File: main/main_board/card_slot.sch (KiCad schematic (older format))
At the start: 6 parts, among them J3 Decimate, P1 my_pcie_8x

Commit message: Checkpoint of state before I start schematic revisions for the next version of the input board. There are not any substantive modifications to the input board, but some broad changes in component attributes related enabling a fabrication quote.
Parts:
- removed C29, C30: 100nF, Capacitor_SMD:C_0603_1608Metric, symbol Device:C_Small
- removed J3: Decimate, Connector_PinHeader_2.00mm:PinHeader_2x02_P2.00mm_Vertical_SMD, symbol Connector_Generic:Conn_02x02_Odd_Even
- removed R27, R28: 3.3K, Resistor_SMD:R_0603_1608Metric, symbol Device:R_US
- P1: footprint input:BUS_PCIexpress_x8 -> input:PCIE_8x_female; Description Do Not Populate -> (none); MPN DNP -> (none)
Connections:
- net labels added: +10V, +5VANA, +5VDIG, -6V, SYNC
- net labels removed: OVDD, RAW_+10V, RAW_+5VANA, RAW_+5VDIG, RAW_-6V, SEL0, SEL1, SYNC_IN
- wire segments 177 -> 155
- no-connect marks 10 -> 7
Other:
- note added: "Connector for a single input board"
- note removed: "Connector is oriented with the low number pins toward\nthe back of the board. Working forward, we have\n -- High speed LVDS signals\n -- Digital supply\n -- Low speed digital signals\n -- Analog supplies\n -- Analog signals\n\nThere are many grounds\n"
- note removed: "Selects the down-sampling factor for the ADC digital filter. \nOn the LTC2512/24 down-sampling factors of 4, 8, 16 and 32 \nare selected for [SEL1 SEL0] combinations of \n00, 01, 10 and 11 respectively."
- note removed: "The connector to the main board, and other support circuitry that\nconnects by global labels"

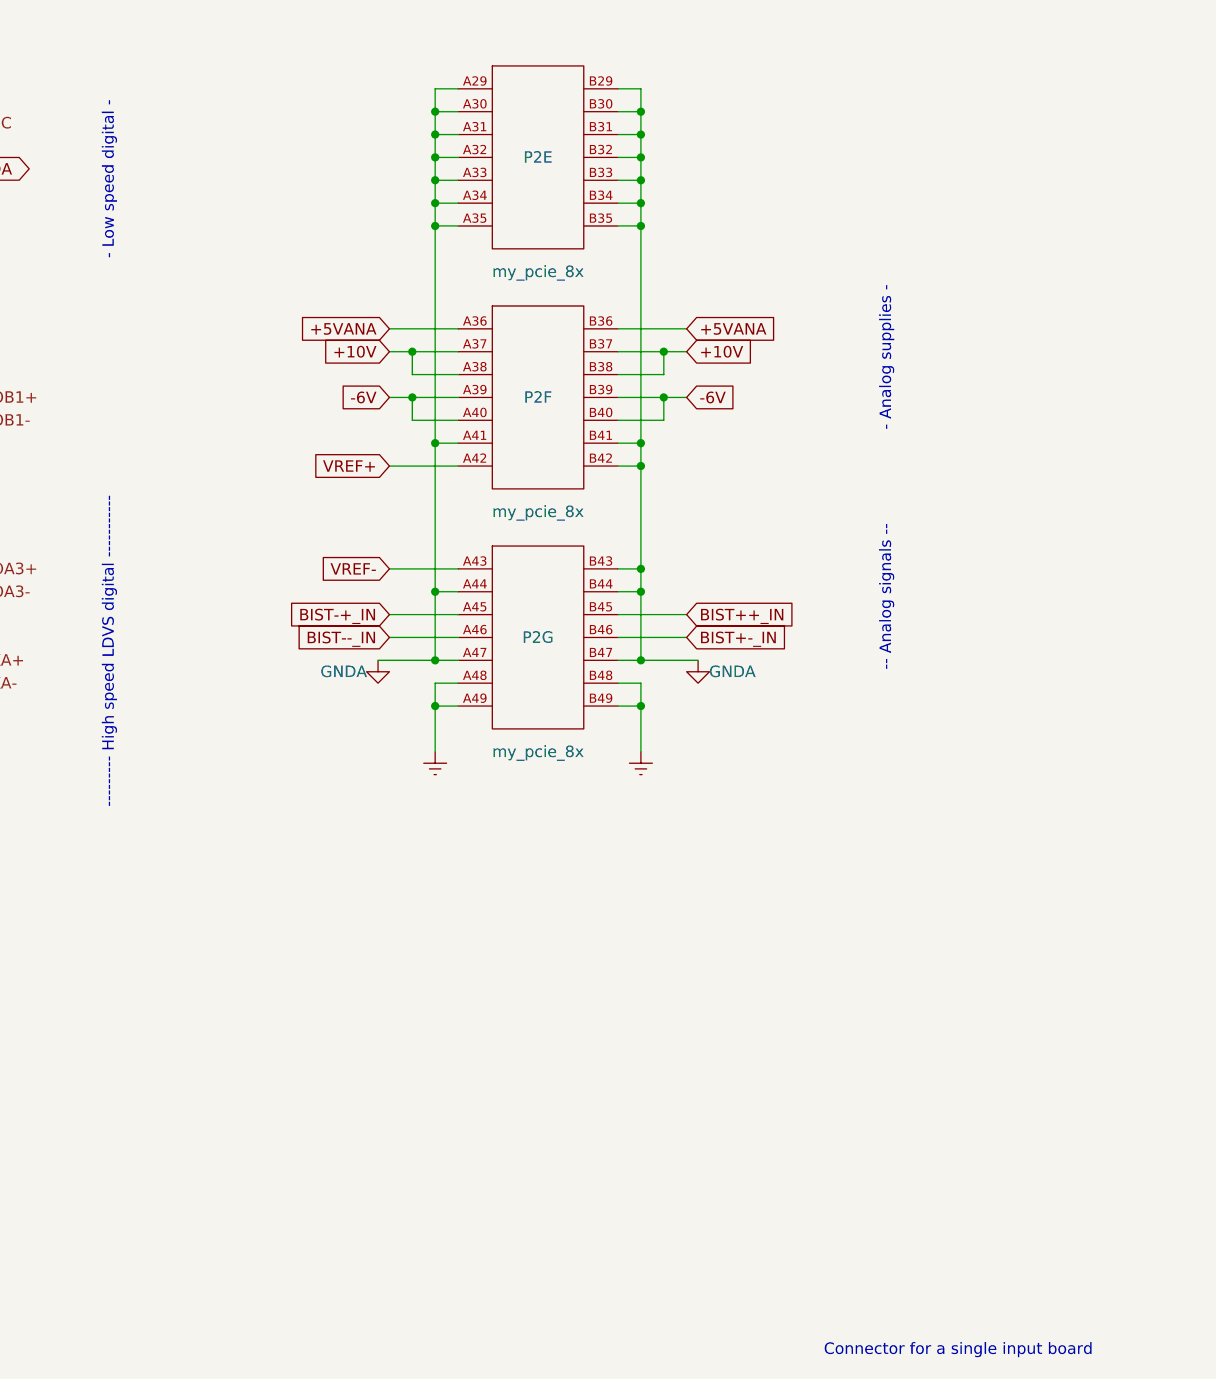
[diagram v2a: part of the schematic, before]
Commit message: A bunch of thinking about RFI and ESD, and some testing.  Mostly reflected in notebook.txt. Also another more explicit round of consideration of box-level grounding and power distribution, because this affects the power conditioning on the main board.  Power nets on the main board are mostly captured.  I added supply decoupling at each plugin slot.
in_filter.sxsch: added simulation of ESD, use vendor models for TVS diode and ferrite.

power_budget.xlsx: get rid of sheets for the input boards not implemented.  Add sheet for
the main board and carry over data from the input board sheet.
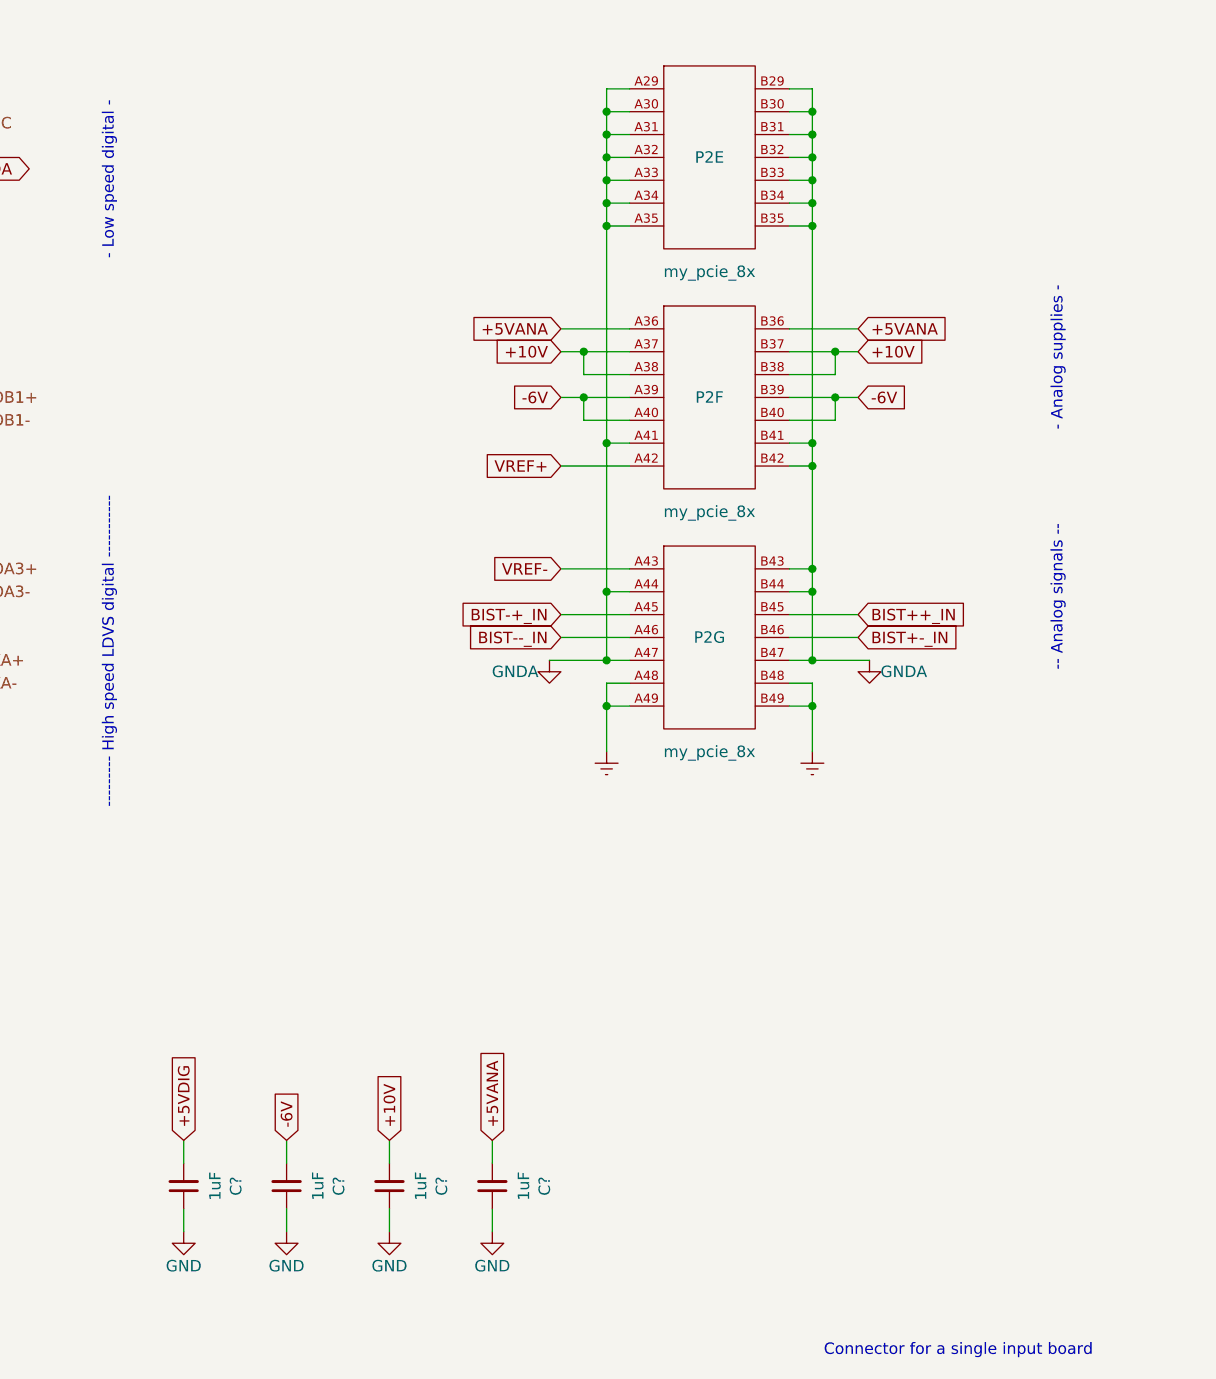
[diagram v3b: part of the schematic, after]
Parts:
- added C? (x4): 1uF, Capacitor_SMD:C_0805_2012Metric, symbol Device:C_Small
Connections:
- net +10V: now also C?.2
- net +5VANA: now also C?.2
- net +5VDIG: now also C?.2
- net -6V: now also C?.2
- net GND: now also C?.1, C?.1, C?.1, C?.1
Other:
- moved on the sheet: P2E, P2F, P2G

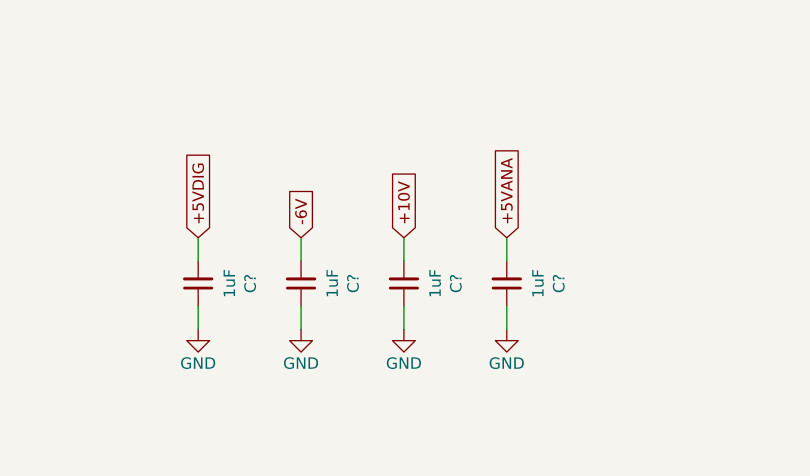
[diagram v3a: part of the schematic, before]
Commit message: Diffs mainly due to first annotation of some new components.  Also changes on power.sch, added TVS and some caps.
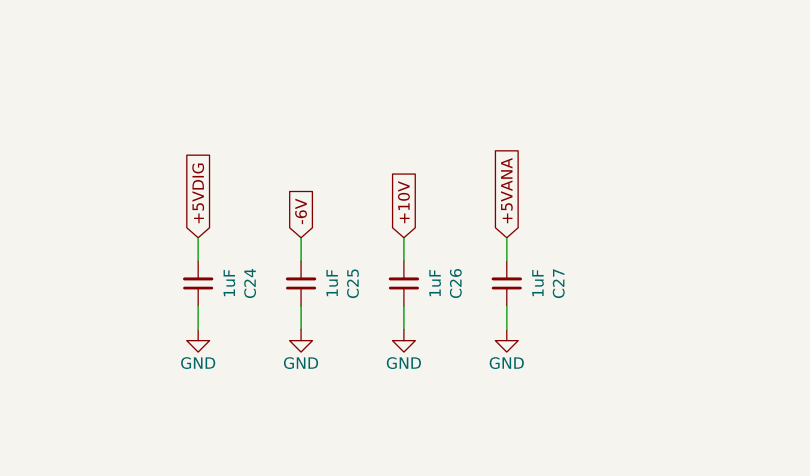
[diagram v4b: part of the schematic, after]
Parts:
- gave numbers to parts that had none: 4
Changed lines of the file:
@@
 AR Path="/5E525F2C/5ED81315" Ref="C?"  Part="1"
 AR Path="/5E525FC9/5ED81315" Ref="C?"  Part="1"
-AR Path="/5E525FFE/5EBAAEAF/5ED81315" Ref="C?"  Part="1"
-F 0 "C?" V 4221 6050 50  0000 C CNN
+AR Path="/5E525FFE/5EBAAEAF/5ED81315" Ref="C24"  Part="1"
+AR Path="/5E525FFE/5EBAAF7D/5ED81315" Ref="C28"  Part="1"
+AR Path="/5E525FFE/5EBAAF8F/5ED81315" Ref="C32"  Part="1"
+AR Path="/5E525FFE/5EBAAFA1/5ED81315" Ref="C36"  Part="1"
+F 0 "C24" V 4221 6050 50  0000 C CNN
 F 1 "1uF" V 4312 6050 50  0000 C CNN
 F 2 "Capacitor_SMD:C_0805_2012Metric" H 4450 6050 50  0001 C CNN
@@
 AR Path="/5E525F2C/5E76E218/5ED8F44E" Ref="#PWR?"  Part="1"
 AR Path="/5E525F2C/5E7721D1/5ED8F44E" Ref="#PWR?"  Part="1"
-AR Path="/5E525FFE/5EBAAEAF/5ED8F44E" Ref="#PWR?"  Part="1"
-AR Path="/5E525FFE/5EBAAF7D/5ED8F44E" Ref="#PWR?"  Part="1"
-AR Path="/5E525FFE/5EBAAF8F/5ED8F44E" Ref="#PWR?"  Part="1"
-AR Path="/5E525FFE/5EBAAFA1/5ED8F44E" Ref="#PWR?"  Part="1"
-F 0 "#PWR?" H 4450 6000 50  0001 C CNN
+AR Path="/5E525FFE/5EBAAEAF/5ED8F44E" Ref="#PWR021"  Part="1"
+AR Path="/5E525FFE/5EBAAF7D/5ED8F44E" Ref="#PWR025"  Part="1"
+AR Path="/5E525FFE/5EBAAF8F/5ED8F44E" Ref="#PWR029"  Part="1"
+AR Path="/5E525FFE/5EBAAFA1/5ED8F44E" Ref="#PWR033"  Part="1"
+F 0 "#PWR021" H 4450 6000 50  0001 C CNN
 F 1 "GND" H 4450 6100 50  0000 C CNN
 F 2 "" H 4450 6250 50  0001 C CNN
@@
 AR Path="/5E525F2C/5EDA5F14" Ref="C?"  Part="1"
 AR Path="/5E525FC9/5EDA5F14" Ref="C?"  Part="1"
-AR Path="/5E525FFE/5EBAAEAF/5EDA5F14" Ref="C?"  Part="1"
-F 0 "C?" V 4671 6050 50  0000 C CNN
+AR Path="/5E525FFE/5EBAAEAF/5EDA5F14" Ref="C25"  Part="1"
+AR Path="/5E525FFE/5EBAAF7D/5EDA5F14" Ref="C29"  Part="1"
+AR Path="/5E525FFE/5EBAAF8F/5EDA5F14" Ref="C33"  Part="1"
+AR Path="/5E525FFE/5EBAAFA1/5EDA5F14" Ref="C37"  Part="1"
+F 0 "C25" V 4671 6050 50  0000 C CNN
 F 1 "1uF" V 4762 6050 50  0000 C CNN
 F 2 "Capacitor_SMD:C_0805_2012Metric" H 4900 6050 50  0001 C CNN
@@
 AR Path="/5E525F2C/5E76E218/5EDA5F1A" Ref="#PWR?"  Part="1"
 AR Path="/5E525F2C/5E7721D1/5EDA5F1A" Ref="#PWR?"  Part="1"
-AR Path="/5E525FFE/5EBAAEAF/5EDA5F1A" Ref="#PWR?"  Part="1"
-AR Path="/5E525FFE/5EBAAF7D/5EDA5F1A" Ref="#PWR?"  Part="1"
-AR Path="/5E525FFE/5EBAAF8F/5EDA5F1A" Ref="#PWR?"  Part="1"
-AR Path="/5E525FFE/5EBAAFA1/5EDA5F1A" Ref="#PWR?"  Part="1"
-F 0 "#PWR?" H 4900 6000 50  0001 C CNN
+AR Path="/5E525FFE/5EBAAEAF/5EDA5F1A" Ref="#PWR022"  Part="1"
+AR Path="/5E525FFE/5EBAAF7D/5EDA5F1A" Ref="#PWR026"  Part="1"
+AR Path="/5E525FFE/5EBAAF8F/5EDA5F1A" Ref="#PWR030"  Part="1"
+AR Path="/5E525FFE/5EBAAFA1/5EDA5F1A" Ref="#PWR034"  Part="1"
+F 0 "#PWR022" H 4900 6000 50  0001 C CNN
 F 1 "GND" H 4900 6100 50  0000 C CNN
 F 2 "" H 4900 6250 50  0001 C CNN
@@
 AR Path="/5E525F2C/5EDBD896" Ref="C?"  Part="1"
 AR Path="/5E525FC9/5EDBD896" Ref="C?"  Part="1"
-AR Path="/5E525FFE/5EBAAEAF/5EDBD896" Ref="C?"  Part="1"
-F 0 "C?" V 5121 6050 50  0000 C CNN
+AR Path="/5E525FFE/5EBAAEAF/5EDBD896" Ref="C26"  Part="1"
+AR Path="/5E525FFE/5EBAAF7D/5EDBD896" Ref="C30"  Part="1"
+AR Path="/5E525FFE/5EBAAF8F/5EDBD896" Ref="C34"  Part="1"
+AR Path="/5E525FFE/5EBAAFA1/5EDBD896" Ref="C38"  Part="1"
+F 0 "C26" V 5121 6050 50  0000 C CNN
 F 1 "1uF" V 5212 6050 50  0000 C CNN
 F 2 "Capacitor_SMD:C_0805_2012Metric" H 5350 6050 50  0001 C CNN
@@
 AR Path="/5E525F2C/5E76E218/5EDBD89C" Ref="#PWR?"  Part="1"
 AR Path="/5E525F2C/5E7721D1/5EDBD89C" Ref="#PWR?"  Part="1"
-AR Path="/5E525FFE/5EBAAEAF/5EDBD89C" Ref="#PWR?"  Part="1"
-AR Path="/5E525FFE/5EBAAF7D/5EDBD89C" Ref="#PWR?"  Part="1"
-AR Path="/5E525FFE/5EBAAF8F/5EDBD89C" Ref="#PWR?"  Part="1"
-AR Path="/5E525FFE/5EBAAFA1/5EDBD89C" Ref="#PWR?"  Part="1"
-F 0 "#PWR?" H 5350 6000 50  0001 C CNN
+AR Path="/5E525FFE/5EBAAEAF/5EDBD89C" Ref="#PWR023"  Part="1"
+AR Path="/5E525FFE/5EBAAF7D/5EDBD89C" Ref="#PWR027"  Part="1"
+AR Path="/5E525FFE/5EBAAF8F/5EDBD89C" Ref="#PWR031"  Part="1"
+AR Path="/5E525FFE/5EBAAFA1/5EDBD89C" Ref="#PWR035"  Part="1"
+F 0 "#PWR023" H 5350 6000 50  0001 C CNN
 F 1 "GND" H 5350 6100 50  0000 C CNN
 F 2 "" H 5350 6250 50  0001 C CNN
@@
 AR Path="/5E525F2C/5EDCC5E2" Ref="C?"  Part="1"
 AR Path="/5E525FC9/5EDCC5E2" Ref="C?"  Part="1"
-AR Path="/5E525FFE/5EBAAEAF/5EDCC5E2" Ref="C?"  Part="1"
-F 0 "C?" V 5571 6050 50  0000 C CNN
+AR Path="/5E525FFE/5EBAAEAF/5EDCC5E2" Ref="C27"  Part="1"
+AR Path="/5E525FFE/5EBAAF7D/5EDCC5E2" Ref="C31"  Part="1"
+AR Path="/5E525FFE/5EBAAF8F/5EDCC5E2" Ref="C35"  Part="1"
+AR Path="/5E525FFE/5EBAAFA1/5EDCC5E2" Ref="C39"  Part="1"
+F 0 "C27" V 5571 6050 50  0000 C CNN
 F 1 "1uF" V 5662 6050 50  0000 C CNN
 F 2 "Capacitor_SMD:C_0805_2012Metric" H 5800 6050 50  0001 C CNN
@@
 AR Path="/5E525F2C/5E76E218/5EDCC5E8" Ref="#PWR?"  Part="1"
 AR Path="/5E525F2C/5E7721D1/5EDCC5E8" Ref="#PWR?"  Part="1"
-AR Path="/5E525FFE/5EBAAEAF/5EDCC5E8" Ref="#PWR?"  Part="1"
-AR Path="/5E525FFE/5EBAAF7D/5EDCC5E8" Ref="#PWR?"  Part="1"
-AR Path="/5E525FFE/5EBAAF8F/5EDCC5E8" Ref="#PWR?"  Part="1"
-AR Path="/5E525FFE/5EBAAFA1/5EDCC5E8" Ref="#PWR?"  Part="1"
-F 0 "#PWR?" H 5800 6000 50  0001 C CNN
+AR Path="/5E525FFE/5EBAAEAF/5EDCC5E8" Ref="#PWR024"  Part="1"
+AR Path="/5E525FFE/5EBAAF7D/5EDCC5E8" Ref="#PWR028"  Part="1"
+AR Path="/5E525FFE/5EBAAF8F/5EDCC5E8" Ref="#PWR032"  Part="1"
+AR Path="/5E525FFE/5EBAAFA1/5EDCC5E8" Ref="#PWR036"  Part="1"
+F 0 "#PWR024" H 5800 6000 50  0001 C CNN
 F 1 "GND" H 5800 6100 50  0000 C CNN
 F 2 "" H 5800 6250 50  0001 C CNN

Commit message: Mostly work on hooking in the Microzed using kipart symbols and a footprint. Also added 2.5V VCCIO regulator.
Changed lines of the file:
@@
 $Descr A4 11693 8268
 encoding utf-8
-Sheet 7 12
+Sheet 10 12
 Title ""
 Date ""
@@
 AR Path="/5E525FFE/5EBAAF8F/5EC152A4" Ref="#PWR089"  Part="1"
 AR Path="/5E525FFE/5EBAAFA1/5EC152A4" Ref="#PWR095"  Part="1"
-F 0 "#PWR077" H 3300 4900 50  0001 C CNN
+F 0 "#PWR095" H 3300 4900 50  0001 C CNN
 F 1 "GND" H 3300 5000 50  0000 C CNN
 F 2 "" H 3300 5150 50  0001 C CNN
@@
 AR Path="/5E525FFE/5EBAAF8F/5EC152A3" Ref="#PWR093"  Part="1"
 AR Path="/5E525FFE/5EBAAFA1/5EC152A3" Ref="#PWR099"  Part="1"
-F 0 "#PWR081" H 7450 3500 50  0001 C CNN
+F 0 "#PWR099" H 7450 3500 50  0001 C CNN
 F 1 "GNDA" H 7600 3700 50  0000 C CNN
 F 2 "" H 7450 3750 50  0001 C CNN
@@
 AR Path="/5E525FFE/5EBAAF8F/5E67C68B" Ref="P4"  Part="3"
 AR Path="/5E525FFE/5EBAAFA1/5E67C68B" Ref="P5"  Part="3"
-F 0 "P2" H 2900 3550 50  0000 C CNN
+F 0 "P5" H 2900 3550 50  0000 C CNN
 F 1 "my_pcie_8x" H 2900 3050 50  0000 C CNN
 F 2 "input:PCIE_8x_female" H 2900 4050 50  0001 C CNN
@@
 AR Path="/5E525FFE/5EBAAF8F/5E682A6A" Ref="P4"  Part="5"
 AR Path="/5E525FFE/5EBAAFA1/5E682A6A" Ref="P5"  Part="5"
-F 0 "P2" H 6750 1550 50  0000 C CNN
+F 0 "P5" H 6750 1550 50  0000 C CNN
 F 1 "my_pcie_8x" H 6750 1050 50  0000 C CNN
 F 2 "input:PCIE_8x_female" H 6750 2050 50  0001 C CNN
@@
 AR Path="/5E525FFE/5EBAAF8F/5E625DE8" Ref="P4"  Part="6"
 AR Path="/5E525FFE/5EBAAFA1/5E625DE8" Ref="P5"  Part="6"
-F 0 "P2" H 6750 2600 50  0000 C CNN
+F 0 "P5" H 6750 2600 50  0000 C CNN
 F 1 "my_pcie_8x" H 6750 2100 50  0000 C CNN
 F 2 "input:PCIE_8x_female" H 6750 3100 50  0001 C CNN
@@
 AR Path="/5E525FFE/5EBAAF8F/5E625DE9" Ref="P4"  Part="7"
 AR Path="/5E525FFE/5EBAAFA1/5E625DE9" Ref="P5"  Part="7"
-F 0 "P2" H 6750 3650 50  0000 C CNN
+F 0 "P5" H 6750 3650 50  0000 C CNN
 F 1 "my_pcie_8x" H 6750 3150 50  0000 C CNN
 F 2 "input:PCIE_8x_female" H 6750 4150 50  0001 C CNN
@@
 AR Path="/5E525FFE/5EBAAF8F/5EC152A6" Ref="P4"  Part="2"
 AR Path="/5E525FFE/5EBAAFA1/5EC152A6" Ref="P5"  Part="2"
-F 0 "P2" H 2900 2500 50  0000 C CNN
+F 0 "P5" H 2900 2500 50  0000 C CNN
 F 1 "my_pcie_8x" H 2900 2000 50  0000 C CNN
 F 2 "input:PCIE_8x_female" H 2900 3000 50  0001 C CNN
@@
 AR Path="/5E525FFE/5EBAAF8F/5E625DEA" Ref="#PWR092"  Part="1"
 AR Path="/5E525FFE/5EBAAFA1/5E625DEA" Ref="#PWR098"  Part="1"
-F 0 "#PWR080" H 7200 3900 50  0001 C CNN
+F 0 "#PWR098" H 7200 3900 50  0001 C CNN
 F 1 "Earth" H 7200 4000 50  0001 C CNN
 F 2 "" H 7200 4150 50  0001 C CNN
@@
 AR Path="/5E525FFE/5EBAAF8F/5E625DEB" Ref="#PWR091"  Part="1"
 AR Path="/5E525FFE/5EBAAFA1/5E625DEB" Ref="#PWR097"  Part="1"
-F 0 "#PWR079" H 6300 3900 50  0001 C CNN
+F 0 "#PWR097" H 6300 3900 50  0001 C CNN
 F 1 "Earth" H 6300 4000 50  0001 C CNN
 F 2 "" H 6300 4150 50  0001 C CNN
@@
 AR Path="/5E525FFE/5EBAAF8F/5E625DEC" Ref="#PWR090"  Part="1"
 AR Path="/5E525FFE/5EBAAFA1/5E625DEC" Ref="#PWR096"  Part="1"
-F 0 "#PWR078" H 6050 3500 50  0001 C CNN
+F 0 "#PWR096" H 6050 3500 50  0001 C CNN
 F 1 "GNDA" H 5900 3700 50  0000 C CNN
 F 2 "" H 6050 3750 50  0001 C CNN
@@
 AR Path="/5E525FFE/5EBAAF8F/5E681104" Ref="P4"  Part="1"
 AR Path="/5E525FFE/5EBAAFA1/5E681104" Ref="P5"  Part="1"
-F 0 "P2" H 2900 1500 50  0000 C CNN
+F 0 "P5" H 2900 1500 50  0000 C CNN
 F 1 "my_pcie_8x" H 2900 1000 50  0000 C CNN
 F 2 "input:PCIE_8x_female" H 2900 2000 50  0001 C CNN
@@
 AR Path="/5E525FFE/5EBAAF8F/5EC152A7" Ref="P4"  Part="4"
 AR Path="/5E525FFE/5EBAAFA1/5EC152A7" Ref="P5"  Part="4"
-F 0 "P2" H 2900 4600 50  0000 C CNN
+F 0 "P5" H 2900 4600 50  0000 C CNN
 F 1 "my_pcie_8x" H 2900 4100 50  0000 C CNN
 F 2 "input:PCIE_8x_female" H 2900 5100 50  0001 C CNN
@@
 AR Path="/5E525FFE/5EBAAF8F/5EC152A5" Ref="#PWR088"  Part="1"
 AR Path="/5E525FFE/5EBAAFA1/5EC152A5" Ref="#PWR094"  Part="1"
-F 0 "#PWR076" H 2500 4900 50  0001 C CNN
+F 0 "#PWR094" H 2500 4900 50  0001 C CNN
 F 1 "GND" H 2500 5000 50  0000 C CNN
 F 2 "" H 2500 5150 50  0001 C CNN
@@
 AR Path="/5E525FFE/5EBAAF8F/5ED81315" Ref="C32"  Part="1"
 AR Path="/5E525FFE/5EBAAFA1/5ED81315" Ref="C36"  Part="1"
-F 0 "C24" V 4221 6050 50  0000 C CNN
+F 0 "C36" V 4221 6050 50  0000 C CNN
 F 1 "1uF" V 4312 6050 50  0000 C CNN
 F 2 "Capacitor_SMD:C_0805_2012Metric" H 4450 6050 50  0001 C CNN
@@
 AR Path="/5E525FFE/5EBAAF8F/5ED8F44E" Ref="#PWR029"  Part="1"
 AR Path="/5E525FFE/5EBAAFA1/5ED8F44E" Ref="#PWR033"  Part="1"
-F 0 "#PWR021" H 4450 6000 50  0001 C CNN
+F 0 "#PWR033" H 4450 6000 50  0001 C CNN
 F 1 "GND" H 4450 6100 50  0000 C CNN
 F 2 "" H 4450 6250 50  0001 C CNN
@@
 AR Path="/5E525FFE/5EBAAF8F/5EDA5F14" Ref="C33"  Part="1"
 AR Path="/5E525FFE/5EBAAFA1/5EDA5F14" Ref="C37"  Part="1"
-F 0 "C25" V 4671 6050 50  0000 C CNN
+F 0 "C37" V 4671 6050 50  0000 C CNN
 F 1 "1uF" V 4762 6050 50  0000 C CNN
 F 2 "Capacitor_SMD:C_0805_2012Metric" H 4900 6050 50  0001 C CNN
@@
 AR Path="/5E525FFE/5EBAAF8F/5EDA5F1A" Ref="#PWR030"  Part="1"
 AR Path="/5E525FFE/5EBAAFA1/5EDA5F1A" Ref="#PWR034"  Part="1"
-F 0 "#PWR022" H 4900 6000 50  0001 C CNN
+F 0 "#PWR034" H 4900 6000 50  0001 C CNN
 F 1 "GND" H 4900 6100 50  0000 C CNN
 F 2 "" H 4900 6250 50  0001 C CNN
@@
 AR Path="/5E525FFE/5EBAAF8F/5EDBD896" Ref="C34"  Part="1"
 AR Path="/5E525FFE/5EBAAFA1/5EDBD896" Ref="C38"  Part="1"
-F 0 "C26" V 5121 6050 50  0000 C CNN
+F 0 "C38" V 5121 6050 50  0000 C CNN
 F 1 "1uF" V 5212 6050 50  0000 C CNN
 F 2 "Capacitor_SMD:C_0805_2012Metric" H 5350 6050 50  0001 C CNN
@@
 AR Path="/5E525FFE/5EBAAF8F/5EDBD89C" Ref="#PWR031"  Part="1"
 AR Path="/5E525FFE/5EBAAFA1/5EDBD89C" Ref="#PWR035"  Part="1"
-F 0 "#PWR023" H 5350 6000 50  0001 C CNN
+F 0 "#PWR035" H 5350 6000 50  0001 C CNN
 F 1 "GND" H 5350 6100 50  0000 C CNN
 F 2 "" H 5350 6250 50  0001 C CNN
@@
 AR Path="/5E525FFE/5EBAAF8F/5EDCC5E2" Ref="C35"  Part="1"
 AR Path="/5E525FFE/5EBAAFA1/5EDCC5E2" Ref="C39"  Part="1"
-F 0 "C27" V 5571 6050 50  0000 C CNN
+F 0 "C39" V 5571 6050 50  0000 C CNN
 F 1 "1uF" V 5662 6050 50  0000 C CNN
 F 2 "Capacitor_SMD:C_0805_2012Metric" H 5800 6050 50  0001 C CNN
@@
 AR Path="/5E525FFE/5EBAAF8F/5EDCC5E8" Ref="#PWR032"  Part="1"
 AR Path="/5E525FFE/5EBAAFA1/5EDCC5E8" Ref="#PWR036"  Part="1"
-F 0 "#PWR024" H 5800 6000 50  0001 C CNN
+F 0 "#PWR036" H 5800 6000 50  0001 C CNN
 F 1 "GND" H 5800 6100 50  0000 C CNN
 F 2 "" H 5800 6250 50  0001 C CNN
